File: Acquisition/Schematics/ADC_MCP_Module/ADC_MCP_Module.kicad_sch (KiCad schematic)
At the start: 39 parts, among them J1 Can, J2 AudioJack4_SwitchTR1, J3 Conn_02x06_Counter_Clockwise, Q1 IRLML9301, SW1 SW_DIP_x01

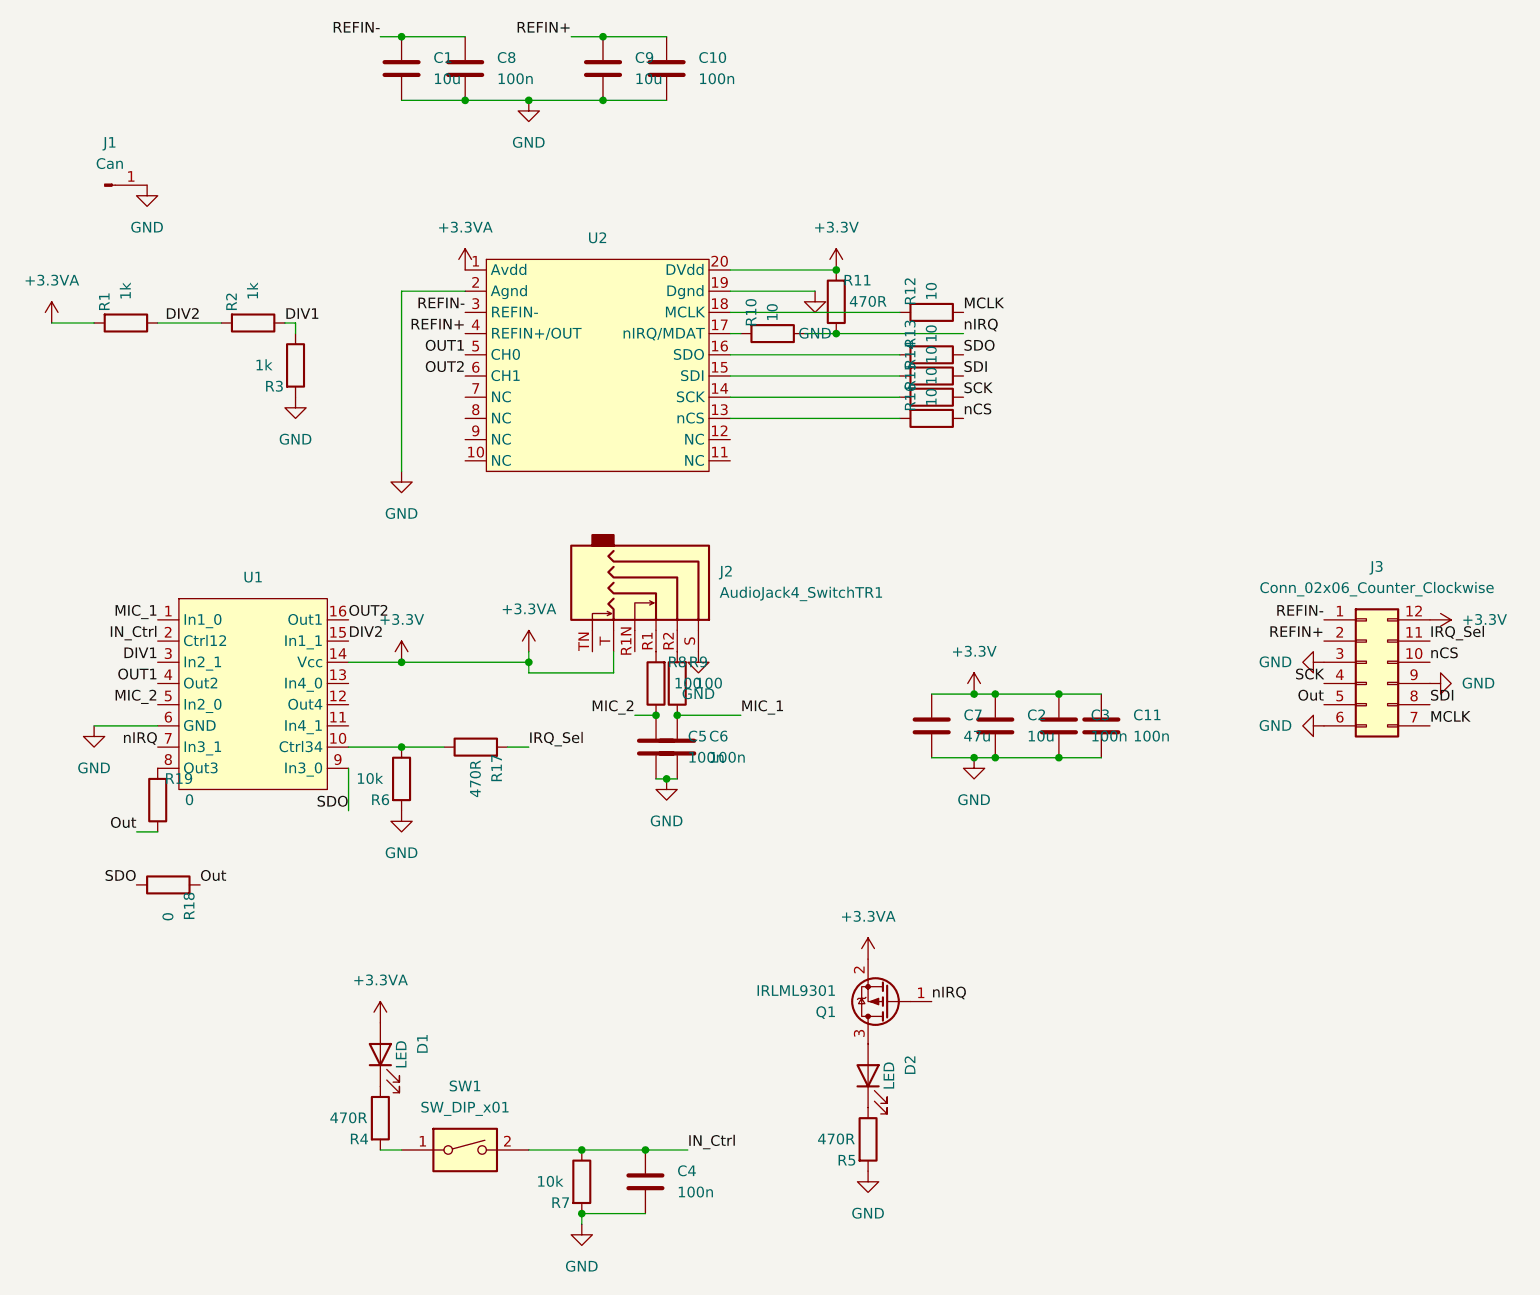
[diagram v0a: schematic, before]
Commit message: Added first version of main board
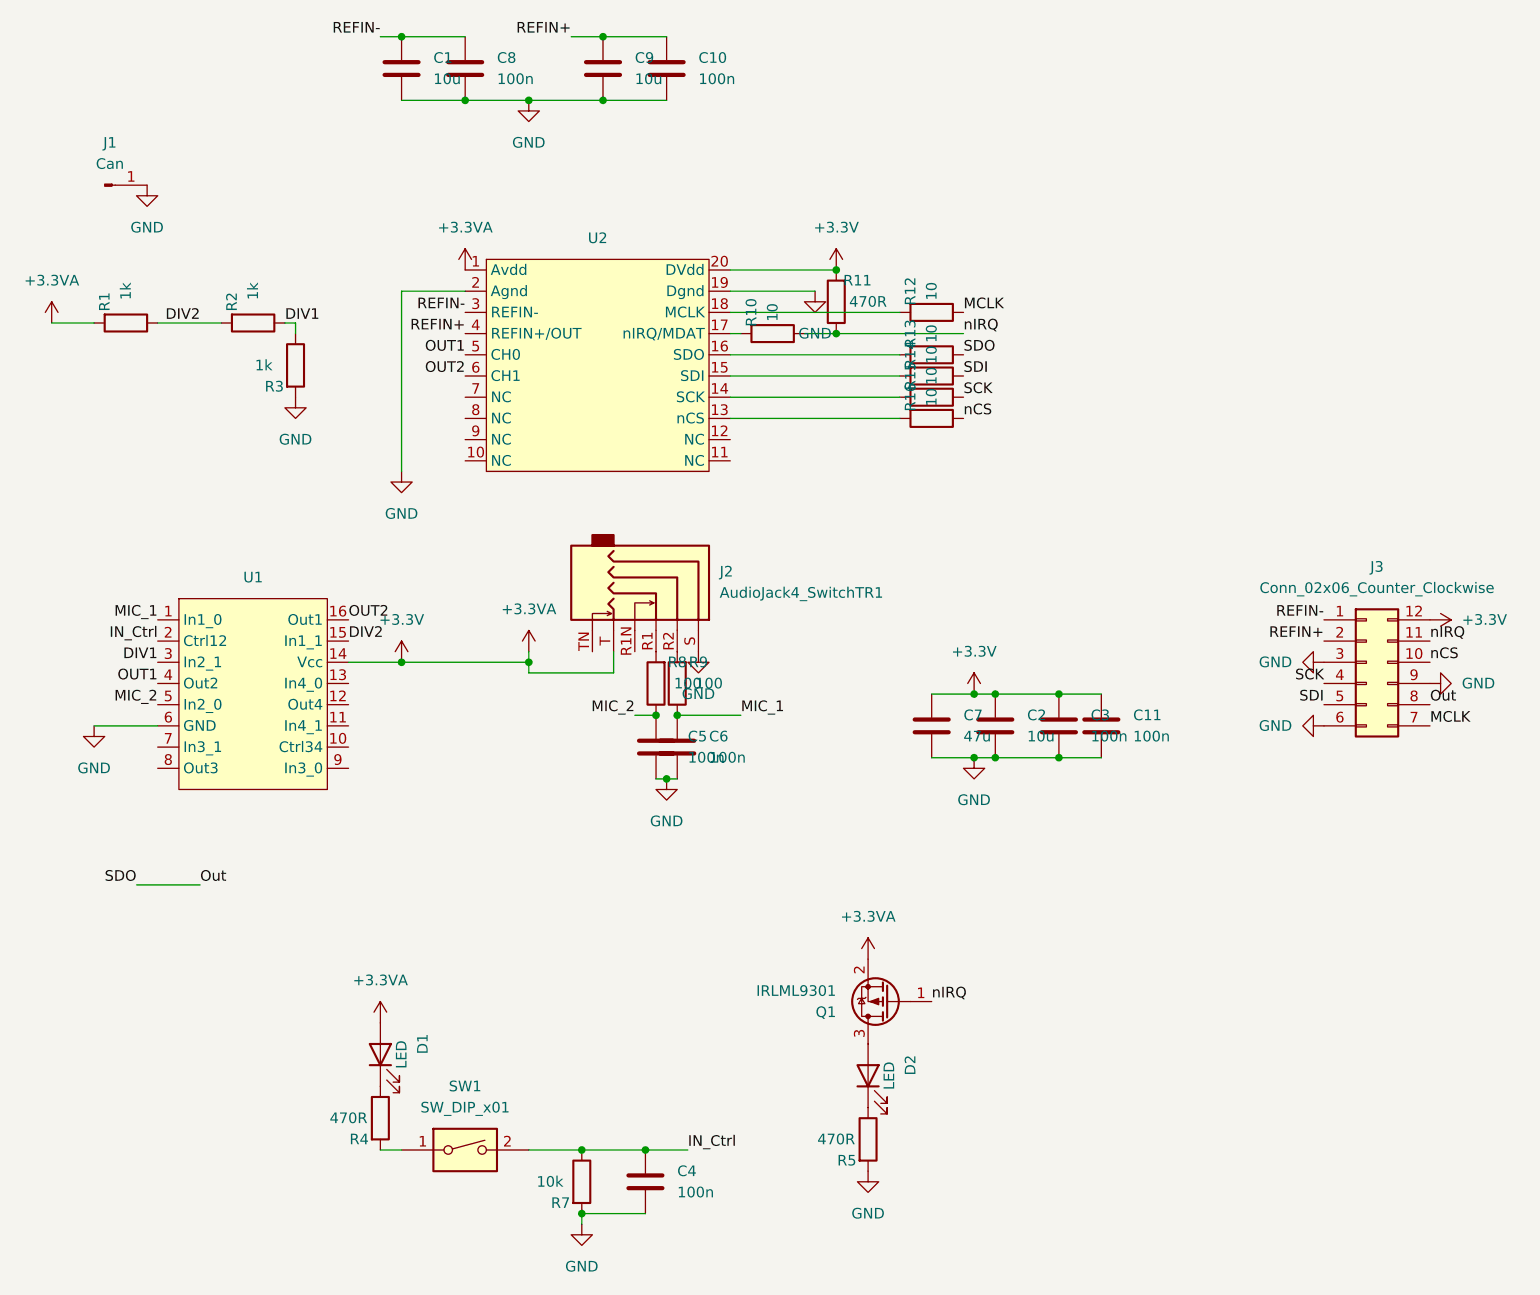
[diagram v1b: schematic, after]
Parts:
- removed R17: 470R, Resistor_SMD:R_0603_1608Metric, symbol Device:R
- removed R18, R19: 0, Resistor_SMD:R_0603_1608Metric, symbol Device:R
- removed R6: 10k, Resistor_SMD:R_0603_1608Metric, symbol Device:R
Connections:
- net IRQ_Sel is gone; now on net nIRQ: J3.11 (Pin_11)
- net Out: now also J3.8 (Pin_8), R13.1; no longer J3.5 (Pin_5)
- net SDI: now also J3.5 (Pin_5); no longer J3.8 (Pin_8)
- net nIRQ: no longer U1.7 (In3_1)
- net SDO: no longer names the net of U1.9 (In3_0)
- net SDO: no longer R13.1
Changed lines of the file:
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@@
   (junction (at 171.45 100.33) (diameter 0) (color 0 0 0 0)
   )
-  (junction (at 92.71 106.68) (diameter 0) (color 0 0 0 0)
-  )
   (junction (at 161.29 100.33) (diameter 0) (color 0 0 0 0)
   )
@@
     (stroke (width 0) (type default))
   )
-  (wire (pts (xy 60.96 116.84) (xy 63.5 116.84))
-    (stroke (width 0) (type default))
-  )
   (wire (pts (xy 55.88 104.14) (xy 63.5 104.14))
     (stroke (width 0) (type default))
@@
     (stroke (width 0) (type default))
   )
-  (wire (pts (xy 92.71 106.68) (xy 97.79 106.68))
-    (stroke (width 0) (type default))
-  )
-  (wire (pts (xy 86.36 109.22) (xy 86.36 114.3))
-    (stroke (width 0) (type default))
-  )
   (wire (pts (xy 132.08 57.15) (xy 133.35 57.15))
     (stroke (width 0) (type default))
@@
     (stroke (width 0) (type default))
   )
-  (wire (pts (xy 92.71 106.68) (xy 86.36 106.68))
-    (stroke (width 0) (type default))
-  )
   (wire (pts (xy 140.97 57.15) (xy 144.78 57.15))
     (stroke (width 0) (type default))
@@
     (stroke (width 0) (type default))
   )
+  (wire (pts (xy 60.96 123.19) (xy 68.58 123.19))
+    (stroke (width 0) (type default))
+  )
   (wire (pts (xy 92.71 29.21) (xy 100.33 29.21))
     (stroke (width 0) (type default))
@@
     (stroke (width 0) (type default))
   )
-  (wire (pts (xy 105.41 106.68) (xy 107.95 106.68))
-    (stroke (width 0) (type default))
-  )
   (wire (pts (xy 116.84 21.59) (xy 124.46 21.59))
     (stroke (width 0) (type default))
@@
     (effects (font (size 1.27 1.27)) (justify right bottom))
   )
-  (label "SDI" (at 215.9 101.6 0) (fields_autoplaced)
-    (effects (font (size 1.27 1.27)) (justify left bottom))
-  )
   (label "DIV2" (at 86.36 93.98 0) (fields_autoplaced)
     (effects (font (size 1.27 1.27)) (justify left bottom))
@@
     (effects (font (size 1.27 1.27)) (justify right bottom))
   )
+  (label "nIRQ" (at 215.9 93.98 0) (fields_autoplaced)
+    (effects (font (size 1.27 1.27)) (justify left bottom))
+  )
   (label "MIC_2" (at 63.5 101.6 180) (fields_autoplaced)
     (effects (font (size 1.27 1.27)) (justify right bottom))
@@
     (effects (font (size 1.27 1.27)) (justify right bottom))
   )
+  (label "SDI" (at 203.2 101.6 180) (fields_autoplaced)
+    (effects (font (size 1.27 1.27)) (justify right bottom))
+  )
   (label "SDI" (at 160.02 62.23 0) (fields_autoplaced)
     (effects (font (size 1.27 1.27)) (justify left bottom))
@@
     (effects (font (size 1.27 1.27)) (justify left bottom))
   )
+  (label "Out" (at 215.9 101.6 0) (fields_autoplaced)
+    (effects (font (size 1.27 1.27)) (justify left bottom))
+  )
   (label "OUT2" (at 100.33 62.23 180) (fields_autoplaced)
     (effects (font (size 1.27 1.27)) (justify right bottom))
@@
     (effects (font (size 1.27 1.27)) (justify left bottom))
   )
-  (label "nIRQ" (at 63.5 106.68 180) (fields_autoplaced)
-    (effects (font (size 1.27 1.27)) (justify right bottom))
-  )
   (label "MIC_1" (at 133.35 102.87 0) (fields_autoplaced)
     (effects (font (size 1.27 1.27)) (justify left bottom))
   )
-  (label "Out" (at 203.2 101.6 180) (fields_autoplaced)
-    (effects (font (size 1.27 1.27)) (justify right bottom))
-  )
   (label "DIV1" (at 63.5 96.52 180) (fields_autoplaced)
     (effects (font (size 1.27 1.27)) (justify right bottom))
   )
-  (label "Out" (at 60.96 116.84 180) (fields_autoplaced)
-    (effects (font (size 1.27 1.27)) (justify right bottom))
-  )
   (label "SCK" (at 160.02 64.77 0) (fields_autoplaced)
     (effects (font (size 1.27 1.27)) (justify left bottom))
@@
     (effects (font (size 1.27 1.27)) (justify right bottom))
   )
-  (label "SDO" (at 86.36 114.3 180) (fields_autoplaced)
-    (effects (font (size 1.27 1.27)) (justify right bottom))
-  )
-  (label "IRQ_Sel" (at 215.9 93.98 0) (fields_autoplaced)
-    (effects (font (size 1.27 1.27)) (justify left bottom))
-  )
   (label "MIC_2" (at 120.65 102.87 180) (fields_autoplaced)
     (effects (font (size 1.27 1.27)) (justify right bottom))
@@
   )
   (label "OUT2" (at 86.36 91.44 0) (fields_autoplaced)
-    (effects (font (size 1.27 1.27)) (justify left bottom))
-  )
-  (label "IRQ_Sel" (at 107.95 106.68 0) (fields_autoplaced)
     (effects (font (size 1.27 1.27)) (justify left bottom))
   )
@@
         (path "/af487b5e-a3f1-4982-9322-f2a7f87ce403"
           (reference "#PWR014") (unit 1)
-        )
-      )
-    )
-  )
-  (symbol (lib_id "Device:R") (at 64.77 123.19 90) (unit 1)
-    (in_bom yes) (on_board yes) (dnp no)
-    (property "Reference" "R18" (at 67.31 125.73 0)
-      (effects (font (size 1.27 1.27)))
-    )
-    (property "Value" "0" (at 64.77 127 0)
-      (effects (font (size 1.27 1.27)))
-    )
-    (property "Footprint" "Resistor_SMD:R_0603_1608Metric" (at 64.77 124.968 90)
-      (effects (font (size 1.27 1.27)) hide)
-    )
-    (property "Datasheet" "~" (at 64.77 123.19 0)
-      (effects (font (size 1.27 1.27)) hide)
-    )
-    (pin "2")
-    (pin "1")
-    (instances
-      (project "ADC_MCP_Module"
-        (path "/af487b5e-a3f1-4982-9322-f2a7f87ce403"
-          (reference "R18") (unit 1)
         )
       )
@@
     )
   )
-  (symbol (lib_id "Device:R") (at 101.6 106.68 90) (unit 1)
-    (in_bom yes) (on_board yes) (dnp no)
-    (property "Reference" "R17" (at 104.14 109.22 0)
-      (effects (font (size 1.27 1.27)))
-    )
-    (property "Value" "470R" (at 101.6 110.49 0)
-      (effects (font (size 1.27 1.27)))
-    )
-    (property "Footprint" "Resistor_SMD:R_0603_1608Metric" (at 101.6 108.458 90)
-      (effects (font (size 1.27 1.27)) hide)
-    )
-    (property "Datasheet" "~" (at 101.6 106.68 0)
-      (effects (font (size 1.27 1.27)) hide)
-    )
-    (pin "2")
-    (pin "1")
-    (instances
-      (project "ADC_MCP_Module"
-        (path "/af487b5e-a3f1-4982-9322-f2a7f87ce403"
-          (reference "R17") (unit 1)
-        )
-      )
-    )
-  )
-  (symbol (lib_id "power:GND") (at 92.71 114.3 0) (unit 1)
-    (in_bom yes) (on_board yes) (dnp no) (fields_autoplaced)
-    (property "Reference" "#PWR018" (at 92.71 120.65 0)
-      (effects (font (size 1.27 1.27)) hide)
-    )
-    (property "Value" "GND" (at 92.71 119.38 0)
-      (effects (font (size 1.27 1.27)))
-    )
-    (property "Footprint" "" (at 92.71 114.3 0)
-      (effects (font (size 1.27 1.27)) hide)
-    )
-    (property "Datasheet" "" (at 92.71 114.3 0)
-      (effects (font (size 1.27 1.27)) hide)
-    )
-    (pin "1")
-    (instances
-      (project "ADC_MCP_Module"
-        (path "/af487b5e-a3f1-4982-9322-f2a7f87ce403"
-          (reference "#PWR018") (unit 1)
-        )
-      )
-    )
-  )
   (symbol (lib_id "power:+3.3V") (at 144.78 49.53 0) (unit 1)
     (in_bom yes) (on_board yes) (dnp no) (fields_autoplaced)
@@
         (path "/af487b5e-a3f1-4982-9322-f2a7f87ce403"
           (reference "SW1") (unit 1)
-        )
-      )
-    )
-  )
-  (symbol (lib_id "Device:R") (at 63.5 113.03 180) (unit 1)
-    (in_bom yes) (on_board yes) (dnp no)
-    (property "Reference" "R19" (at 66.04 110.49 0)
-      (effects (font (size 1.27 1.27)))
-    )
-    (property "Value" "0" (at 67.31 113.03 0)
-      (effects (font (size 1.27 1.27)))
-    )
-    (property "Footprint" "Resistor_SMD:R_0603_1608Metric" (at 65.278 113.03 90)
-      (effects (font (size 1.27 1.27)) hide)
-    )
-    (property "Datasheet" "~" (at 63.5 113.03 0)
-      (effects (font (size 1.27 1.27)) hide)
-    )
-    (pin "2")
-    (pin "1")
-    (instances
-      (project "ADC_MCP_Module"
-        (path "/af487b5e-a3f1-4982-9322-f2a7f87ce403"
-          (reference "R19") (unit 1)
         )
       )
@@
         )
       )
-    )
-  )
-  (symbol (lib_id "Device:R") (at 92.71 110.49 0) (unit 1)
-    (in_bom yes) (on_board yes) (dnp no)
-    (property "Reference" "R6" (at 90.17 113.03 0)
-      (effects (font (size 1.27 1.27)))
-    )
-    (property "Value" "10k" (at 88.9 110.49 0)
-      (effects (font (size 1.27 1.27)))
-    )
-    (property "Footprint" "Resistor_SMD:R_0603_1608Metric" (at 90.932 110.49 90)
-      (effects (font (size 1.27 1.27)) hide)
-    )
-    (property "Datasheet" "~" (at 92.71 110.49 0)
-      (effects (font (size 1.27 1.27)) hide)
-    )
-    (pin "2")
-    (pin "1")
-    (instances
-      (project "ADC_MCP_Module"
-        (path "/af487b5e-a3f1-4982-9322-f2a7f87ce403"
-          (reference "R6") (unit 1)
-        )
-      )
